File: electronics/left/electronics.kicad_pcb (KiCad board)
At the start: 2 copper layers, 109.6 x 73.9 mm, 90 parts, among them J1 USB_C_Receptacle_USB2.0, J2 Battery Connector, SW1 Choc v1 Socket, SW10 Choc v1 Socket, SW11 Choc v1 Socket, SW12 Choc v1 Socket, SW13 Choc v1 Socket, SW14 Choc v1 Socket, SW15 Choc v1 Socket, SW16 Choc v1 Socket, SW17 Choc v1 Socket, SW18 Choc v1 Socket, SW19 Choc v1 Socket, SW2 Choc v1 Socket, SW20 Choc v1 Socket, SW21 Choc v1 Socket, SW22 SW_Reset, SW3 Choc v1 Socket, SW4 Choc v1 Socket, SW5 Choc v1 Socket, SW6 Choc v1 Socket, SW7 Choc v1 Socket, SW8 Choc v1 Socket, SW9 Choc v1 Socket, U1 nRF52840, U2 ESDR0502NMUTAG, U3 BQ24075RGT, Y1 32.768 kHz, Y2 32MHz

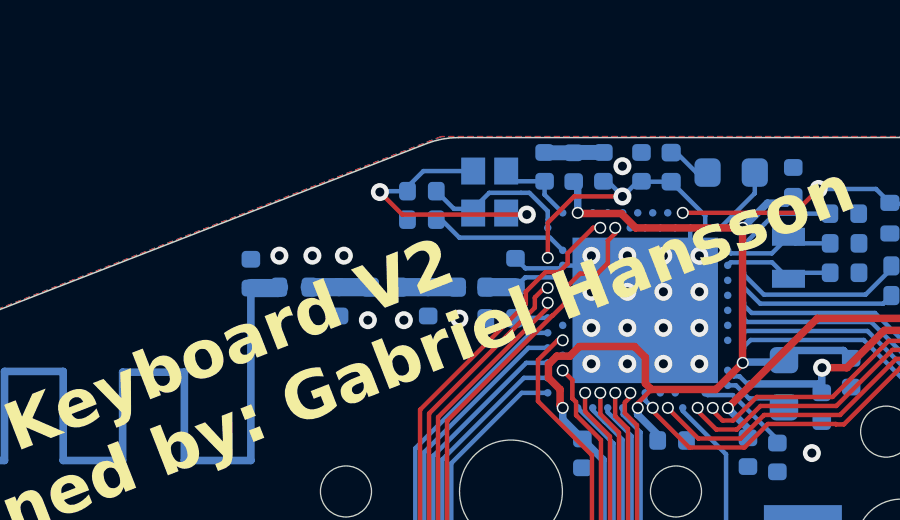
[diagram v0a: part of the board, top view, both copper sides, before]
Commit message: Mouse bite clearance accomodation.
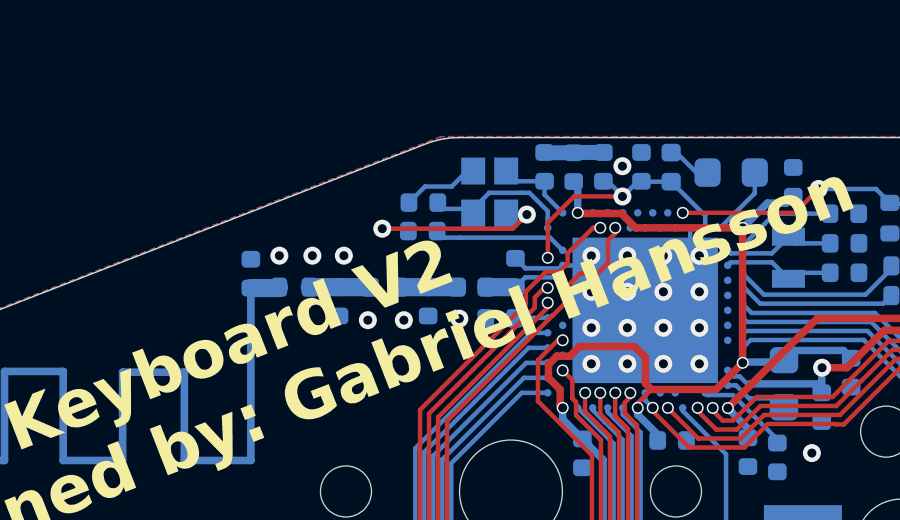
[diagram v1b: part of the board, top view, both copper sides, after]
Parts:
- moved C21 0.38 mm to (69.1, 28.1)
- moved C12 0.38 mm to (69.1, 29.0)
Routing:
- net GND: track 45.8 -> 44.7 mm

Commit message: electronics/left: Fix schema and PCB references parity.
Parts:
- C1, C10, C11, C12, C13, C14, C15, C16, C17, C18, C19, C2, C20, C21, C22, C23, C24, C25, C26, C3, C4, C5, C6, C7, C8, C9: footprint lib:C_0402_1005Metric -> Capacitor_SMD:C_0402_1005Metric
- J2: value Battery Connector -> Molex_781710002
- R1, R10, R11, R12, R2, R3, R4, R5, R6, R7, R8, R9: footprint lib:R_0402_1005Metric -> Resistor_SMD:R_0402_1005Metric
- SW1, SW10, SW11, SW12, SW13, SW14, SW15, SW16, SW17, SW18, SW19, SW2, SW20, SW21, SW3, SW4, SW5, SW6, SW7, SW8, SW9: value Choc v1 Socket -> CPG135001S30
- SW22: value SW_Reset -> EVQPUC02K
- U2: value ESDR0502NMUTAG -> UDFN6-6_1.2x1.0mm_P0.4mm
- U3: footprint lib:VQFN-16-1EP_3x3mm_P0.5mm_EP1.6x1.6mm -> Package_DFN_QFN:VQFN-16-1EP_3x3mm_P0.5mm_EP1.6x1.6mm
- moved SW21 102.5 mm to (126.1, 93.7), turned to 0 degrees
- moved SW1 91.3 mm to (36.0, 44.7)
- moved SW18 91.3 mm to (126.1, 76.7), turned to 0 degrees
- moved SW7 75.3 mm to (36.0, 61.7)
- moved SW15 61.3 mm to (72.1, 71.7), turned to 0 degrees
- moved SW9 58.3 mm to (72.1, 54.7), turned to 180 degrees
- moved SW5 56.9 mm to (108.1, 39.7), turned to 180 degrees
- moved SW11 54.2 mm to (108.1, 56.7)
- moved SW14 44.4 mm to (54.1, 78.7), turned to 0 degrees
- moved SW4 37.1 mm to (90.1, 35.7)
- moved SW3 36.7 mm to (72.1, 37.7), turned to 180 degrees
- moved SW6 35.8 mm to (126.1, 42.7), turned to 180 degrees
- moved SW2 34.0 mm to (54.1, 44.7), turned to 180 degrees
- moved SW16 34.0 mm to (90.1, 69.7), turned to 0 degrees
- moved SW8 30.0 mm to (54.1, 61.7)
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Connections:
- SW1 pad 1: K12 -> K1
- SW10 pad 1: K9 -> K10
- SW11 pad 1: K8 -> K11
- SW12 pad 1: K11 -> K12
- SW14 pad 1: K10 -> K14
- SW15 pad 1: K6 -> K15
- SW16 pad 1: K4 -> K16
- SW17 pad 1: K20 -> K17
- SW18 pad 1: K7 -> K18
- SW19 pad 1: K15 -> K19
- SW2 pad 1: K14 -> K2
- SW20 pad 1: K19 -> K20
- SW21 pad 1: K1 -> K21
- SW3 pad 1: K16 -> K3
- SW4 pad 1: K2 -> K4
- SW5 pad 1: K21 -> K5
- SW6 pad 1: K17 -> K6
- SW7 pad 1: K5 -> K7
- SW8 pad 1: K3 -> K8
- SW9 pad 1: K18 -> K9
